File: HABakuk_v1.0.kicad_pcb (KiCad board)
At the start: 4 copper layers, 38.7 x 48.1 mm, 59 parts, among them J1 ICSP, J10 C-, J2 I2C, J3 SERIAL, J4 GPS_Ant, J5 ANT_UP, J6 ANT_DWN, J7 SOL+, J8 SOL-, J9 C+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

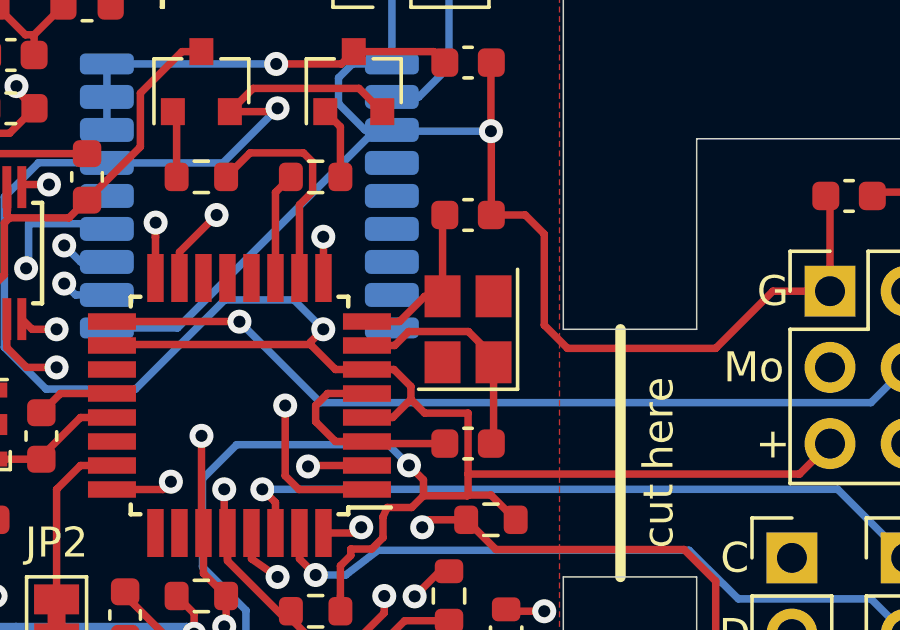
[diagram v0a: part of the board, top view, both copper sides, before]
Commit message: Added BOMs, modified 8 MHz crystal footprint
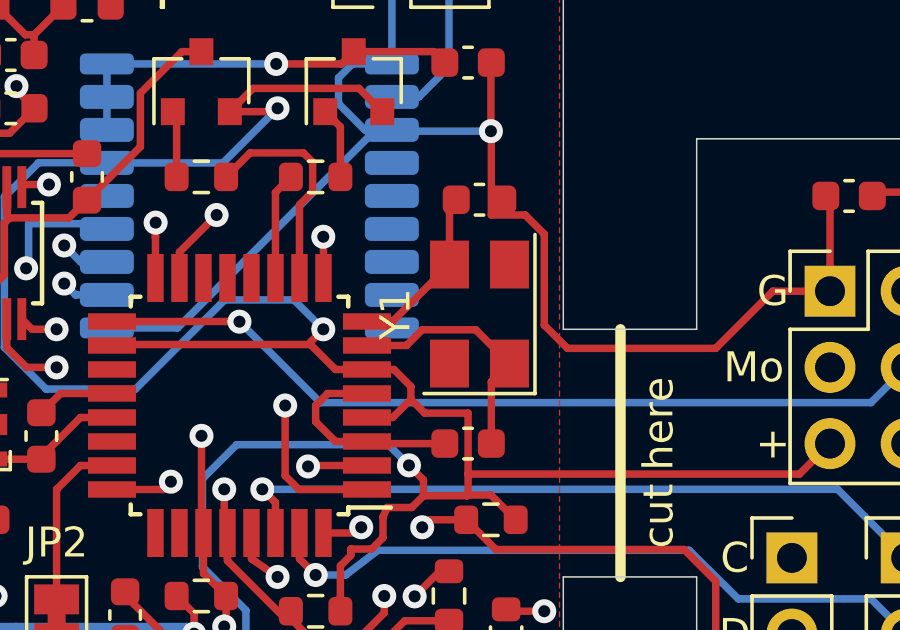
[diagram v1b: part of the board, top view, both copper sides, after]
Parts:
- C14: value 0,47 -> 0,47u
- Y1: footprint Crystal:Crystal_SMD_Abracon_ABM8G-4Pin_3.2x2.5mm -> Crystal:Crystal_SMD_5032-4Pin_5.0x3.2mm
- moved C12 0.63 mm to (133.7, 94.7)
- moved Y1 0.63 mm to (133.7, 98.6)
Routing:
- net Net-(C11-Pad1): track 7.69 -> 8.35 mm
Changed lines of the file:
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@@
     (thickness 0.8)
     (drawings 56)
-    (tracks 483)
+    (tracks 481)
     (zones 0)
     (modules 59)
@@
     (34 B.Paste user)
     (35 F.Paste user)
-    (36 B.SilkS user)
+    (36 B.SilkS user hide)
     (37 F.SilkS user)
     (38 B.Mask user)
@@
     (add_net VDD_TST)
   )
+  (module Crystal:Crystal_SMD_5032-4Pin_5.0x3.2mm (layer F.Cu)
+    (at 133.731 98.552 90)
+    (descr "SMD Crystal SERIES SMD2520/4 http://www.icbase.com/File/PDF/HKC/HKC00061008.pdf, 5.0x3.2mm^2 package")
+    (tags "SMD SMT crystal")
+    (attr smd)
+    (fp_text reference Y1 (at 0 -2.8 90) (layer F.SilkS)
+      (effects (font (size 1 1) (thickness 0.15)))
+    )
+    (fp_text value Crystal_GND24_Small (at 0 2.8 90) (layer F.Fab)
+      (effects (font (size 1 1) (thickness 0.15)))
+    )
+    (fp_text user %R (at 0 0 90) (layer F.Fab)
+      (effects (font (size 1 1) (thickness 0.15)))
+    )
+    (fp_line (start -2.3 -1.6) (end 2.3 -1.6) (layer F.Fab) (width 0.1))
+    (fp_line (start 2.3 -1.6) (end 2.5 -1.4) (layer F.Fab) (width 0.1))
+    (fp_line (start 2.5 -1.4) (end 2.5 1.4) (layer F.Fab) (width 0.1))
+    (fp_line (start 2.5 1.4) (end 2.3 1.6) (layer F.Fab) (width 0.1))
+    (fp_line (start 2.3 1.6) (end -2.3 1.6) (layer F.Fab) (width 0.1))
+    (fp_line (start -2.3 1.6) (end -2.5 1.4) (layer F.Fab) (width 0.1))
+    (fp_line (start -2.5 1.4) (end -2.5 -1.4) (layer F.Fab) (width 0.1))
+    (fp_line (start -2.5 -1.4) (end -2.3 -1.6) (layer F.Fab) (width 0.1))
+    (fp_line (start -2.5 0.6) (end -1.5 1.6) (layer F.Fab) (width 0.1))
+    (fp_line (start -2.65 -1.85) (end -2.65 1.85) (layer F.SilkS) (width 0.12))
+    (fp_line (start -2.65 1.85) (end 2.65 1.85) (layer F.SilkS) (width 0.12))
+    (fp_line (start -2.8 -1.9) (end -2.8 1.9) (layer F.CrtYd) (width 0.05))
+    (fp_line (start -2.8 1.9) (end 2.8 1.9) (layer F.CrtYd) (width 0.05))
+    (fp_line (start 2.8 1.9) (end 2.8 -1.9) (layer F.CrtYd) (width 0.05))
+    (fp_line (start 2.8 -1.9) (end -2.8 -1.9) (layer F.CrtYd) (width 0.05))
+    (pad 4 smd rect (at -1.65 -1 90) (size 1.6 1.3) (layers F.Cu F.Paste F.Mask)
+      (net 59 "Net-(Y1-Pad4)"))
+    (pad 3 smd rect (at 1.65 -1 90) (size 1.6 1.3) (layers F.Cu F.Paste F.Mask)
+      (net 11 "Net-(C12-Pad1)"))
+    (pad 2 smd rect (at 1.65 1 90) (size 1.6 1.3) (layers F.Cu F.Paste F.Mask)
+      (net 60 "Net-(Y1-Pad2)"))
+    (pad 1 smd rect (at -1.65 1 90) (size 1.6 1.3) (layers F.Cu F.Paste F.Mask)
+      (net 10 "Net-(C11-Pad1)"))
+    (model ${KISYS3DMOD}/Crystal.3dshapes/Crystal_SMD_5032-4Pin_5.0x3.2mm.wrl
+      (at (xyz 0 0 0))
+      (scale (xyz 1 1 1))
+      (rotate (xyz 0 0 0))
+    )
+  )
   (module _moje_footprints:STMITE (layer F.Cu)
     (at 127.508 116.205)
@@
     )
     (pad "" np_thru_hole circle (at 0 0) (size 2.1 2.1) (drill 2.1) (layers *.Cu *.Mask))
-  )
-  (module Crystal:Crystal_SMD_Abracon_ABM8G-4Pin_3.2x2.5mm (layer F.Cu)
-    (at 133.35 99.06 90)
-    (descr "Abracon Miniature Ceramic Smd Crystal ABM8G http://www.abracon.com/Resonators/ABM8G.pdf, 3.2x2.5mm^2 package")
-    (tags "SMD SMT crystal")
-    (attr smd)
-    (fp_text reference Y1 (at 0 -2.45 90) (layer F.SilkS) hide
-      (effects (font (size 1 1) (thickness 0.15)))
-    )
-    (fp_text value Crystal_GND24_Small (at 0 2.45 90) (layer F.Fab)
-      (effects (font (size 1 1) (thickness 0.15)))
-    )
-    (fp_line (start 2.1 -1.7) (end -2.1 -1.7) (layer F.CrtYd) (width 0.05))
-    (fp_line (start 2.1 1.7) (end 2.1 -1.7) (layer F.CrtYd) (width 0.05))
-    (fp_line (start -2.1 1.7) (end 2.1 1.7) (layer F.CrtYd) (width 0.05))
-    (fp_line (start -2.1 -1.7) (end -2.1 1.7) (layer F.CrtYd) (width 0.05))
-    (fp_line (start -2 1.65) (end 2 1.65) (layer F.SilkS) (width 0.12))
-    (fp_line (start -2 -1.65) (end -2 1.65) (layer F.SilkS) (width 0.12))
-    (fp_line (start -1.6 0.25) (end -0.6 1.25) (layer F.Fab) (width 0.1))
-    (fp_line (start -1.6 -1.05) (end -1.4 -1.25) (layer F.Fab) (width 0.1))
-    (fp_line (start -1.6 1.05) (end -1.6 -1.05) (layer F.Fab) (width 0.1))
-    (fp_line (start -1.4 1.25) (end -1.6 1.05) (layer F.Fab) (width 0.1))
-    (fp_line (start 1.4 1.25) (end -1.4 1.25) (layer F.Fab) (width 0.1))
-    (fp_line (start 1.6 1.05) (end 1.4 1.25) (layer F.Fab) (width 0.1))
-    (fp_line (start 1.6 -1.05) (end 1.6 1.05) (layer F.Fab) (width 0.1))
-    (fp_line (start 1.4 -1.25) (end 1.6 -1.05) (layer F.Fab) (width 0.1))
-    (fp_line (start -1.4 -1.25) (end 1.4 -1.25) (layer F.Fab) (width 0.1))
-    (fp_text user %R (at 0 0 90) (layer F.Fab)
-      (effects (font (size 0.7 0.7) (thickness 0.105)))
-    )
-    (pad 4 smd rect (at -1.1 -0.85 90) (size 1.4 1.2) (layers F.Cu F.Paste F.Mask)
-      (net 59 "Net-(Y1-Pad4)"))
-    (pad 3 smd rect (at 1.1 -0.85 90) (size 1.4 1.2) (layers F.Cu F.Paste F.Mask)
-      (net 11 "Net-(C12-Pad1)"))
-    (pad 2 smd rect (at 1.1 0.85 90) (size 1.4 1.2) (layers F.Cu F.Paste F.Mask)
-      (net 60 "Net-(Y1-Pad2)"))
-    (pad 1 smd rect (at -1.1 0.85 90) (size 1.4 1.2) (layers F.Cu F.Paste F.Mask)
-      (net 10 "Net-(C11-Pad1)"))
-    (model ${KISYS3DMOD}/Crystal.3dshapes/Crystal_SMD_Abracon_ABM8G-4Pin_3.2x2.5mm.wrl
-      (at (xyz 0 0 0))
-      (scale (xyz 1 1 1))
-      (rotate (xyz 0 0 0))
-    )
   )
   (module Package_TO_SOT_SMD:SOT-23-5 (layer F.Cu)
@@
       (effects (font (size 1 1) (thickness 0.15)))
     )
-    (fp_text value 0,47 (at 0 1.43) (layer F.Fab)
+    (fp_text value 0,47u (at 0 1.43) (layer F.Fab)
       (effects (font (size 1 1) (thickness 0.15)))
     )
@@
   )
   (module Capacitor_SMD:C_0603_1608Metric (layer F.Cu)
-    (at 133.35 95.25)
+    (at 133.731 94.742)
     (descr "Capacitor SMD 0603 (1608 Metric), square (rectangular) end terminal, IPC_7351 nominal, (Body size source: IPC-SM-782 page 76, https://www.pcb-3d.com/wordpress/wp-content/uploads/ipc-sm-782a_amendment_1_and_2.pdf), generated with kicad-footprint-generator")
     (tags capacitor)
@@
   (segment (start 119.767 101.2) (end 121.48 101.2) (width 0.25) (layer F.Cu) (net 9))
   (segment (start 119.126 101.841) (end 119.767 101.2) (width 0.25) (layer F.Cu) (net 9))
-  (segment (start 129.98 99.6) (end 130.905 99.6) (width 0.25) (layer F.Cu) (net 10))
-  (segment (start 134.2 99.974998) (end 134.2 100.16) (width 0.25) (layer F.Cu) (net 10))
-  (segment (start 133.360001 99.134999) (end 134.2 99.974998) (width 0.25) (layer F.Cu) (net 10))
-  (segment (start 131.370001 99.134999) (end 133.360001 99.134999) (width 0.25) (layer F.Cu) (net 10))
-  (segment (start 130.905 99.6) (end 131.370001 99.134999) (width 0.25) (layer F.Cu) (net 10))
-  (segment (start 134.2 102.795) (end 134.125 102.87) (width 0.25) (layer F.Cu) (net 10))
-  (segment (start 134.2 100.16) (end 134.2 102.795) (width 0.25) (layer F.Cu) (net 10))
-  (segment (start 131.90859 97.96) (end 132.5 97.96) (width 0.25) (layer F.Cu) (net 11))
-  (segment (start 131.06859 98.8) (end 131.90859 97.96) (width 0.25) (layer F.Cu) (net 11))
-  (segment (start 129.98 98.8) (end 131.06859 98.8) (width 0.25) (layer F.Cu) (net 11))
-  (segment (start 132.5 95.325) (end 132.575 95.25) (width 0.25) (layer F.Cu) (net 11))
-  (segment (start 132.5 97.96) (end 132.5 95.325) (width 0.25) (layer F.Cu) (net 11))
+  (segment (start 133.605999 99.076999) (end 134.731 100.202) (width 0.25) (layer F.Cu) (net 10))
+  (segment (start 131.820999 99.076999) (end 133.605999 99.076999) (width 0.25) (layer F.Cu) (net 10))
+  (segment (start 131.297998 99.6) (end 131.820999 99.076999) (width 0.25) (layer F.Cu) (net 10))
+  (segment (start 129.98 99.6) (end 131.297998 99.6) (width 0.25) (layer F.Cu) (net 10))
+  (segment (start 134.125 100.808) (end 134.731 100.202) (width 0.25) (layer F.Cu) (net 10))
+  (segment (start 134.125 102.87) (end 134.125 100.808) (width 0.25) (layer F.Cu) (net 10))
+  (segment (start 130.833 98.8) (end 132.731 96.902) (width 0.25) (layer F.Cu) (net 11))
+  (segment (start 129.98 98.8) (end 130.833 98.8) (width 0.25) (layer F.Cu) (net 11))
+  (segment (start 132.731 94.967) (end 132.956 94.742) (width 0.25) (layer F.Cu) (net 11))
+  (segment (start 132.731 96.902) (end 132.731 94.967) (width 0.25) (layer F.Cu) (net 11))
   (segment (start 132.21 89.805) (end 132.575 90.17) (width 0.25) (layer F.Cu) (net 12))
   (segment (start 129.54 89.805) (end 132.21 89.805) (width 0.25) (layer F.Cu) (net 12))
